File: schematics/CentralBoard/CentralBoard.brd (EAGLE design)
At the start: 97.1 x 89.8 mm, 67 parts, among them CON1 XT30UPB-M, CON2 XT30UPB-M, CON3 XT30UPB-M, CON4 XT30UPB-M, CON5 XT30UPB-M, CON6 XT30UPB-M, CON7 XT30UPB-M, CON8 XT30UPB-M, IC2 SN75C3232, IC3 LTC7001, P10 Power Switch, P11 Foot4, P12 Foot3, P13 Foot2, P14 Foot1, P2 ODrive1, P3 MAIN_SPI, P4 IMU, P5 ODrive2, P6 ODrive3, P7 ODrive4, P8 ODrive5, P9 ODrive6, U2 INA226AIDGST

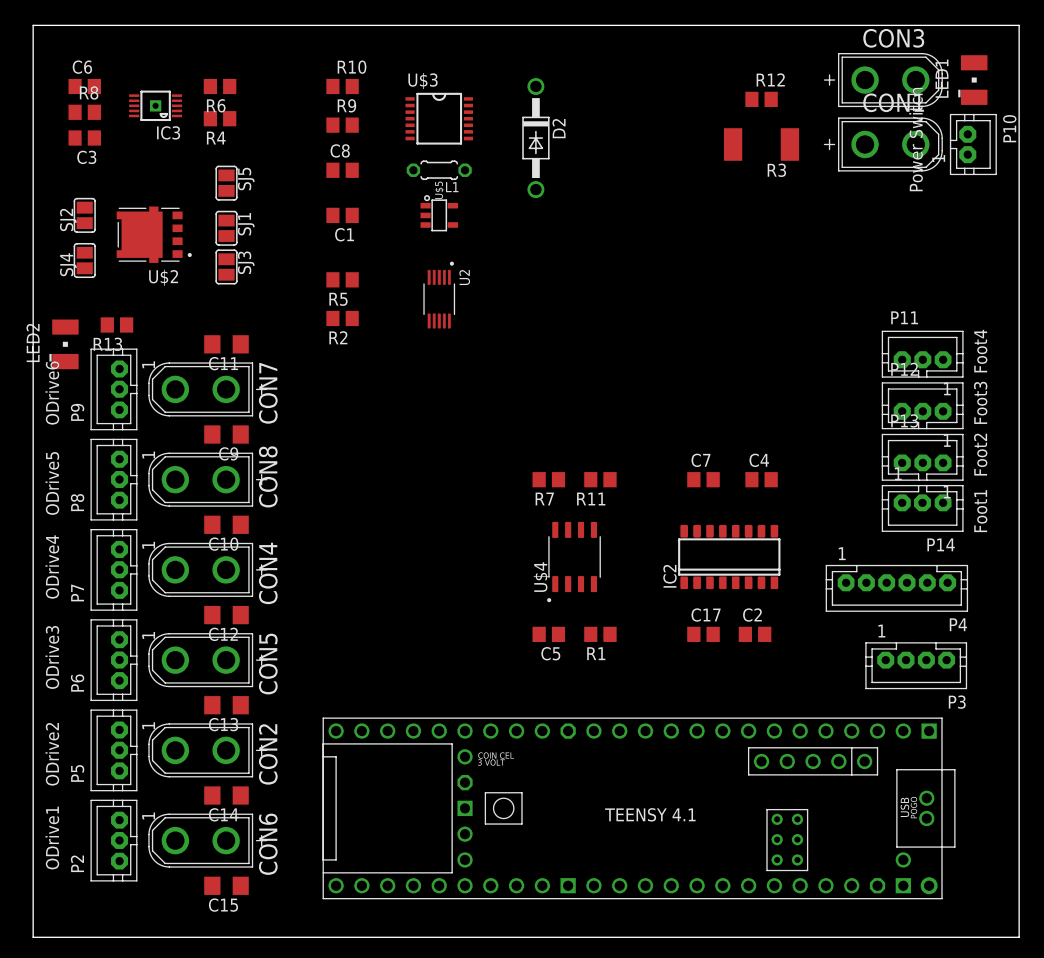
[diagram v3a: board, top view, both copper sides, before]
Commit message: removed old SMD version
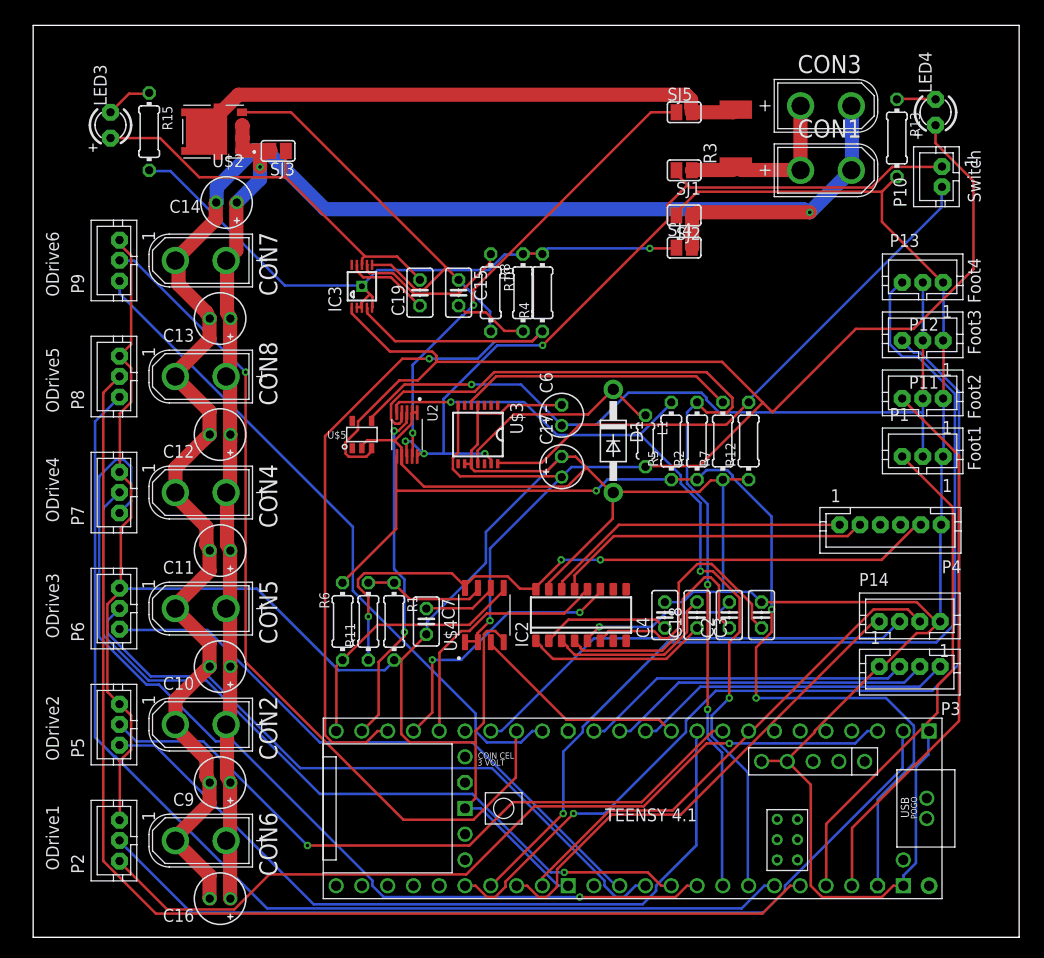
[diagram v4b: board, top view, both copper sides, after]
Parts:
- removed C1: 1uF, rcl:C0805
- removed C5: 1nF, rcl:C0805
- removed C8: 10uF, rcl:C0805
- removed D2: 1N4004, diode:DO41-10
- removed LED1: Power, led:PLCC2
- removed LED2: P-ODrive, led:PLCC2
- removed R9: 47k, rcl:R0805
- added C16: 2.2uF, rcl:E2-5
- added C18: 100nF, rcl:C025-025X050
- added C19: 4.7uF, rcl:C025-025X050
- added D1: (no value), adafruit:DO41-10
- added LED3: P-ODrive, adafruit:LED3MM
- added LED4: ON, adafruit:LED3MM
- added P1: Foot1, jst-ph:JST-PH3
- added R15: 1k, rcl:0204/7
- C10, C11, C12, C13, C14, C9: device rcl:C1206 -> rcl:E2-5
- C15: value 2.2uF -> 0.47uF#; device rcl:C1206 -> rcl:C025-025X050
- C17: value 100nF -> 10uF; device rcl:C0805 -> rcl:E2-4
- C2, C4: device rcl:C0805 -> rcl:C025-025X050
- C3: value 4.7uF -> 100nF; device rcl:C0805 -> rcl:C025-025X050
- C6: value 0.47uF -> 1uF; device rcl:C0805 -> rcl:E2-4
- C7: value 100nF -> 1nF; device rcl:C0805 -> rcl:C025-025X050
- P10: value Power Switch -> Switch
- P11: value Foot4 -> Foot2
- P13: value Foot2 -> Foot4
- P14: value Foot1 -> SPI2; device jst-ph:JST-PH3 -> jst-ph:JST-PH4
- P3: value MAIN_SPI -> SPI
- R1: value 100K -> 10K; device rcl:R0805 -> rcl:0204/7
- R10, R13, R2, R5: device rcl:R0805 -> rcl:0204/7
- R11: value 100K -> 100k; device rcl:R0805 -> rcl:0204/7
- R12: value 1K -> 100k; device rcl:R0805 -> rcl:0204/7
- R4: value 10K -> 10k; device rcl:R0805 -> rcl:0204/7
- R6: value 10K -> 100k; device rcl:R0805 -> rcl:0204/7
- R7: value 10K -> 47k; device rcl:R0805 -> rcl:0204/7
- R8: value 100K -> 10; device rcl:R0805 -> rcl:0204/7
- moved C3 81.6 mm to (71.8, 31.8), turned to 90 degrees
- moved R13 79.0 mm to (85.1, 78.7), turned to 270 degrees
- moved C15 62.7 mm to (41.9, 63.5), turned to 270 degrees
- moved SJ4 59.1 mm to (64.1, 67.9), turned to 0 degrees
- moved SJ2 59.1 mm to (64.1, 71.1), turned to 180 degrees
- moved C14 58.4 mm to (19.1, 72.4)
- moved C6 57.1 mm to (52.1, 51.4), turned to 90 degrees
- moved R6 54.1 mm to (30.5, 31.1), turned to 90 degrees
- moved R8 46.7 mm to (48.3, 63.5), turned to 90 degrees
- moved SJ5 45.6 mm to (64.1, 81.3), turned to 0 degrees
- moved SJ1 45.4 mm to (64.1, 75.6), turned to 180 degrees
- moved C13 38.1 mm to (18.4, 61.0)
- moved R2 37.0 mm to (65.4, 48.9), turned to 90 degrees
- moved R4 36.1 mm to (50.2, 63.5), turned to 90 degrees
- moved R5 36.1 mm to (62.9, 48.9), turned to 90 degrees
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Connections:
- net SENSOR3 renamed SENS3
- removed net SENSOR1: P14.3, U$1.22-A8/CTX1
- removed net SENSOR2: P13.3, U$1.23-A9/CRX1/MCLK1
- removed net SENSOR4: P11.3, U$1.39-A15/CS/OUT1A
- new net CS1: P14.4, U$1.40-A16/CS1
- new net MISO1: P14.2, U$1.41-A17/MISO1
- new net MOSI1: P14.3, U$1.26-A12/MOSI1
- new net SCK1: U$1.27-A13/SCK1
- new net SENS1: P1.3, U$1.22-A8/CTX1
- new net SENS2: P11.3, U$1.23-A9/CRX1/MCLK1
- new net SENS4: P13.3, U$1.39-A15/CS/OUT1A
- net +3.3V: now also C6.+, P1.2; no longer C1.1, P14.2
- net +5V: now also C17.+, LED4.A; no longer C8.1, LED1.A
- net BATT-: now also C10.-, C11.-, C12.-, C13.-, C14.-, C16.-, C9.-; no longer C10.2, C11.2, C12.2, C13.2, C14.2, C15.2, C9.2
- net GND: now also C17.-, C3.2, C6.-, D1.A, P1.1, R1.2, R13.2; no longer C1.2, C5.2, C8.2, D2.A, R10.1, R9.1
- net IMU_VDD: now also R6.1; no longer R11.1
- net N$10: now also R4.1; no longer R4.2
- net N$13: now also C4.1; no longer C7.1
- net N$14: now also C3.1; no longer C4.1
- net N$15: now also R15.2, R4.2, R8.2; no longer R13.1, R4.1, R6.1
- net N$16: now also C15.2, R8.1; no longer C6.2, R6.2
- net N$17: now also R5.2; no longer R2.1
- net N$19: now also C15.1, R10.2; no longer C6.1, R8.1
- net N$2: now also LED4.K, R13.1; no longer LED1.C, R12.2
- net N$20: now also R12.2; no longer R10.2
- net N$21: now also C10.+, C11.+, C12.+, C13.+, C14.+, C16.+, C9.+; no longer C10.1, C11.1, C12.1, C13.1, C14.1, C15.1, C9.1
- net N$22: now also R2.2; no longer R5.1
- net N$23: now also R2.1, R5.1, R6.2; no longer R11.2, R2.2, R5.2
- net N$24: now also C19.1; no longer C3.1
- net N$25: now also R11.2; no longer R7.2
- net N$26: now also C19.2, LED3.A; no longer C3.2, LED2.A
- net N$27: now also R7.2; no longer R9.2
- net N$29: now also D1.C; no longer D2.C
- net N$3: now also C7.1; no longer C5.1
- net N$30: now also LED3.K, R15.1; no longer LED2.C, R13.2
- net N$31: now also R11.1; no longer R1.2
- net N$4: now also R10.1; no longer R8.2
- net N$6: now also C18.1; no longer C17.1
- net N$8: now also C18.2; no longer C17.2
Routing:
- net GND: track 0.00 -> 429.0 mm
- net BATT-: track 0.00 -> 176.2 mm, vias 0 -> 1
- net +5V: track 0.00 -> 166.3 mm, vias 0 -> 1
- net O5_RX: track 0.00 -> 120.3 mm
- net O5_TX: track 0.00 -> 109.4 mm
- net N$23: track 0.00 -> 107.0 mm, vias 0 -> 3
- net SENS4: track 0.00 -> 98.0 mm, vias 0 -> 1
- net O4_TX: track 0.00 -> 95.2 mm, vias 0 -> 1
- net N$22: track 0.00 -> 94.3 mm, vias 0 -> 2
- net SENS3: track 0.00 -> 94.1 mm, vias 0 -> 1
- net O1_RX: track 0.00 -> 90.0 mm
- net O6_RX: track 0.00 -> 85.0 mm, vias 0 -> 1
- net O1_TX: track 0.00 -> 84.0 mm, vias 0 -> 1
- net N$17: track 0.00 -> 82.7 mm, vias 0 -> 3
- net N$21: track 0.00 -> 82.1 mm, vias 0 -> 1
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
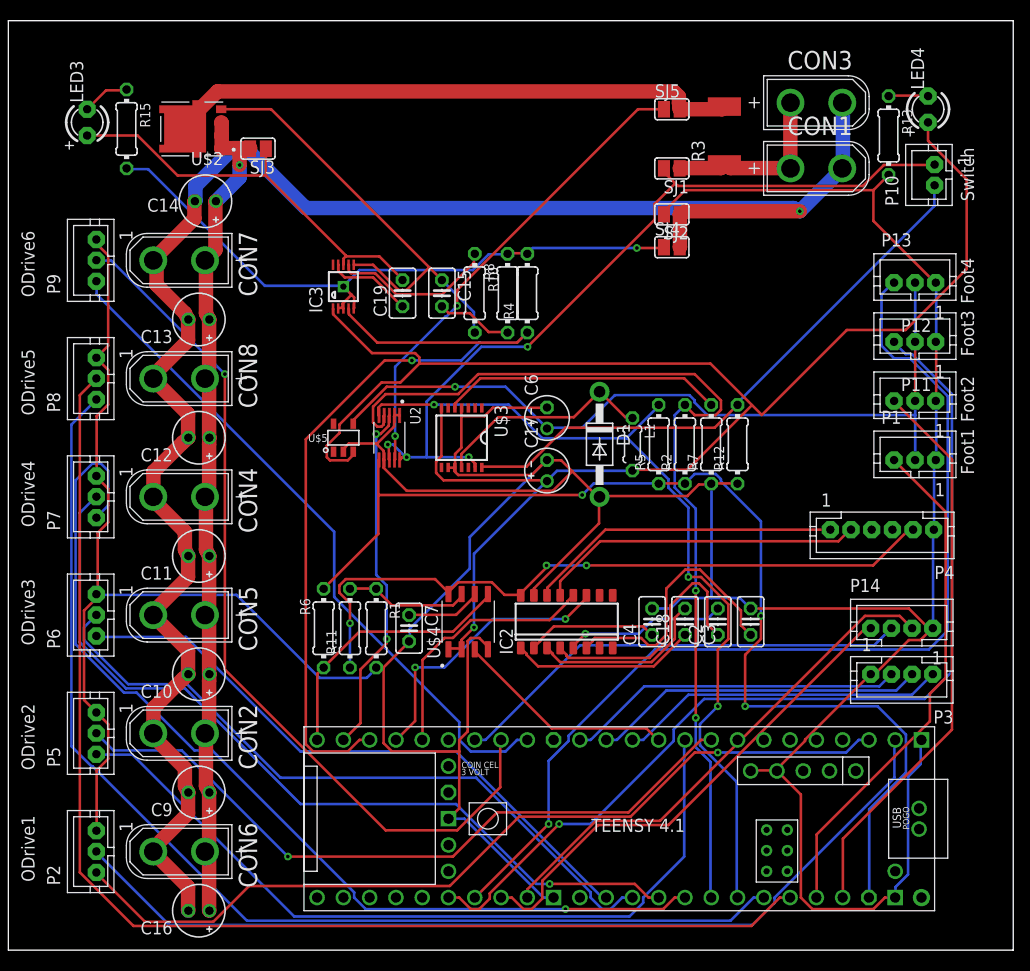
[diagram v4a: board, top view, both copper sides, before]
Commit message: new head and tail
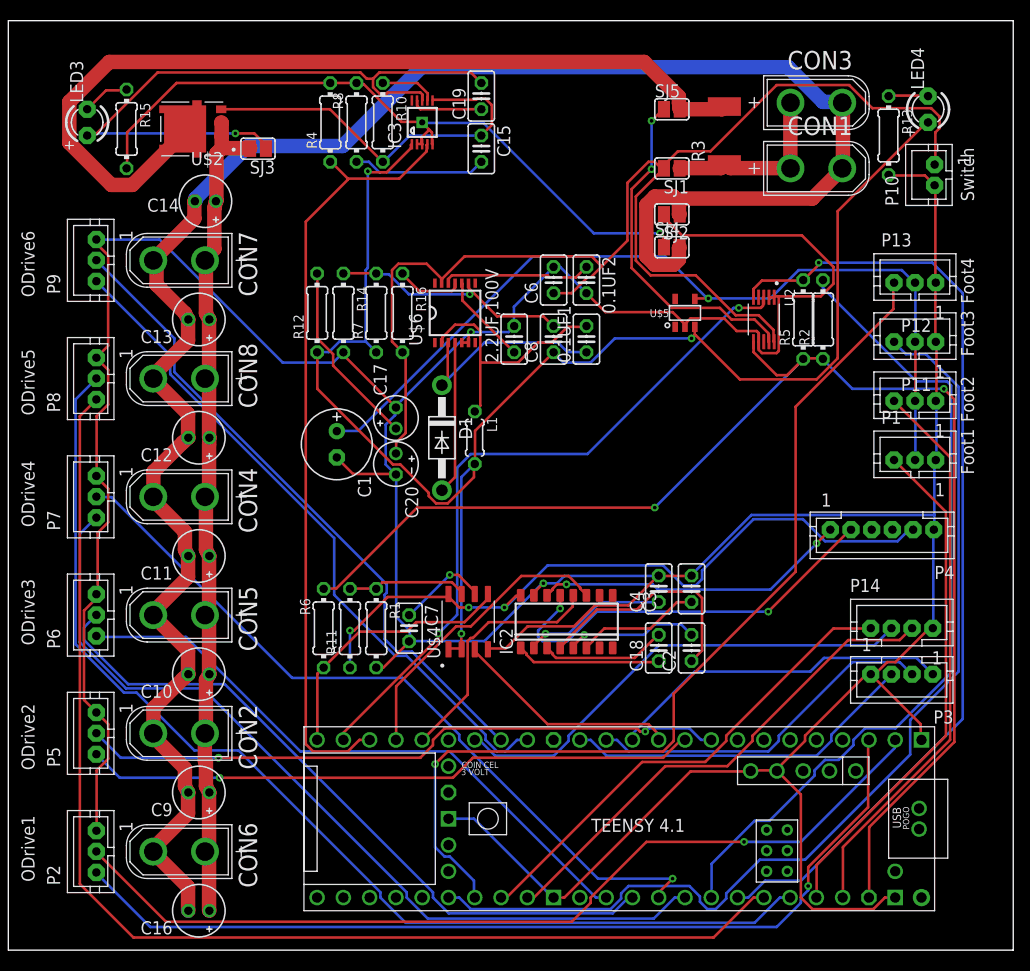
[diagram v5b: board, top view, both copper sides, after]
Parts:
- removed U$3: TLF50211EL, TLF50211EL:TSSOP-14
- added 0.1UF1: 22nF, rcl:C025-025X050
- added 0.1UF2: 100nF, rcl:C025-025X050
- added 2.2UF,100V: 4.7uF, rcl:C025-025X050
- added C1: 220V, rcl:E2,5-7
- added C20: 4.7uF, rcl:E2-4
- added C8: 10nF, rcl:C025-025X050
- added R14: 4.7k, rcl:0204/7
- added R16: 200k, rcl:0204/7
- added U$6: LM5010, LM5010:TSSOP-14
- C17: value 10uF -> 22uF
- C6: value 1uF -> 100nF; device rcl:E2-4 -> rcl:C025-025X050
- D1: value (none) -> 2A, 100V
- L1: value 10uH -> 50uH
- R12: value 100k -> 2
- R7: value 47k -> 4.7K
- moved R12 42.6 mm to (29.8, 61.6)
- moved U2 38.0 mm to (73.0, 61.0)
- moved U$5 35.2 mm to (65.4, 61.6)
- moved R7 34.8 mm to (35.6, 61.6)
- moved R4 25.2 mm to (31.1, 80.0)
- moved R8 22.0 mm to (33.7, 80.0)
- moved C19 20.5 mm to (45.7, 82.5)
- moved R10 18.8 mm to (36.2, 80.0)
- moved R5 18.5 mm to (76.8, 61.0)
- moved R2 18.0 mm to (78.7, 61.0)
- moved IC3 17.6 mm to (40.0, 80.0)
- moved C17 15.5 mm to (37.5, 51.4)
- moved D1 15.3 mm to (41.9, 49.5)
- moved L1 15.3 mm to (45.1, 49.5)
- moved C15 14.5 mm to (45.7, 77.5)
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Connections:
- new net LED_PWM: U$1.5-IN2
- new net N$33: 2.2UF,100V.1, U$6.10
- new net N$34: 0.1UF2.1, U$6.12
- new net N$35: 0.1UF1.2, L1.1, U$6.2
- new net N$36: C8.2, R14.1, R7.2, U$6.9
- new net N$37: D1.A, U$6.4
- net +3.3V: now also C1.+; no longer C6.+
- net +5V: now also C8.1, R12.1, R7.1; no longer C17.+, U$3.7
- net BATT: now also C20.+, C6.1, R16.2, U$6.13; no longer U$3.13
- net GND: now also 0.1UF2.2, 2.2UF,100V.2, C1.-, C20.-, C6.2, P10.2, R14.2, U$6.5, U$6.6; no longer C6.-, D1.A, R12.1, R7.1, U$3.10, U$3.4, U$3.9
- net N$20: now also C17.+; no longer P10.2, U$3.14
- net N$27: now also R16.1, U$6.11; no longer R7.2, U$3.5
- net N$29: now also 0.1UF1.1, U$6.3; no longer L1.1, U$3.11
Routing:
- net BATT: track 78.9 -> 124.7 mm, vias 4 -> 0
- net N$20: track 56.3 -> 18.1 mm
- net N$5: track 34.3 -> 67.8 mm
- net N$9: track 55.1 -> 87.4 mm
- net N$26: track 39.8 -> 66.3 mm, vias 0 -> 1
- net N$35: track 0.00 -> 24.8 mm
- net N$23: track 107.0 -> 130.9 mm, vias 3 -> 2
- net N$36: track 0.00 -> 23.7 mm, vias 0 -> 1
- net O6_RX: track 85.0 -> 63.6 mm, vias 1 -> 0
- net N$27: track 27.3 -> 6.42 mm
- net +5V: track 166.3 -> 147.3 mm, vias 1 -> 3
- net O2_TX: track 77.4 -> 59.4 mm, vias 0 -> 1
- net BATT-: track 176.2 -> 193.1 mm, vias 1 -> 0
- net N$37: track 0.00 -> 14.8 mm
- net N$22: track 94.3 -> 79.5 mm, vias 2 -> 0
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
